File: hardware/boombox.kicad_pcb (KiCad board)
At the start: 4 copper layers, 97.7 x 88.3 mm, 74 parts, among them J1 Micro_SD_Card_Det1, J2 AudioJack4, J3 Battery, J4 USB_C_Receptacle_USB2.0_16P, SW1 SW_SPST, SW2 SW_SPST, SW3 SW_SPST, SW4 SW_SPST, SW5 SW_SPST, U1 Pico, U10 MAX98365A, U2 TMAG5231, U3 TMAG5231, U4 TMAG5231, U5 TMAG5231, U6 TMAG5231, U7 MCP7940MT-I/SN, U8 MAX98365A, U9 MCP73811T-420I-OT, Y1 Crystal

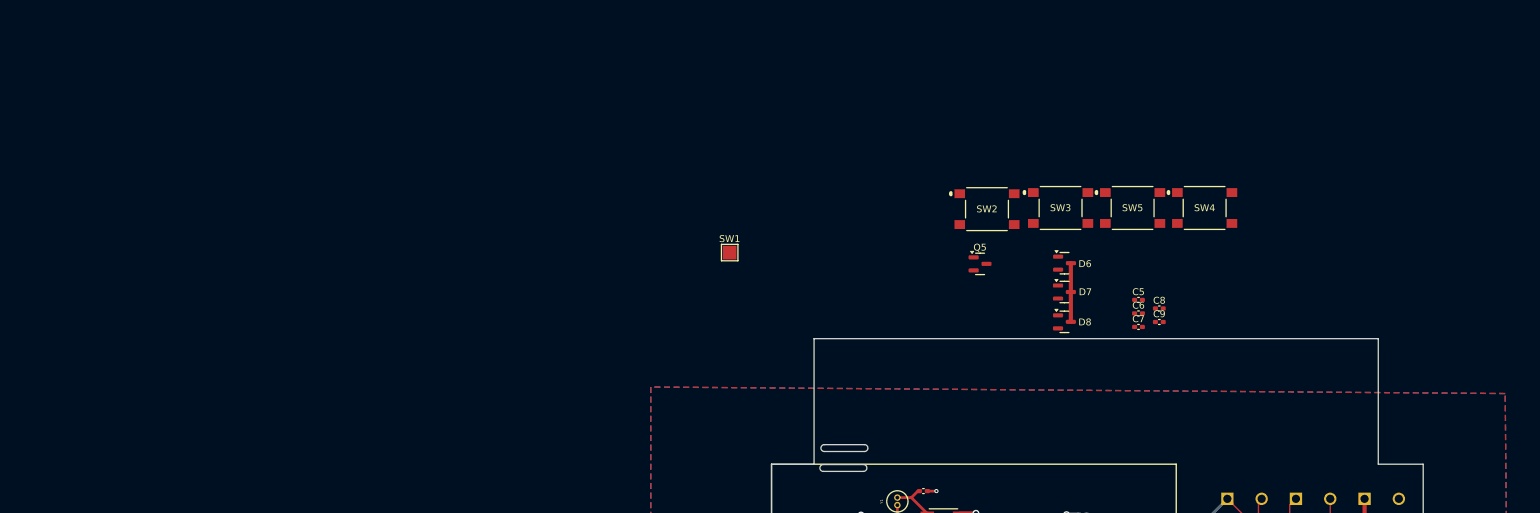
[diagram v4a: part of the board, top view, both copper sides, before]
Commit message: Added button panel
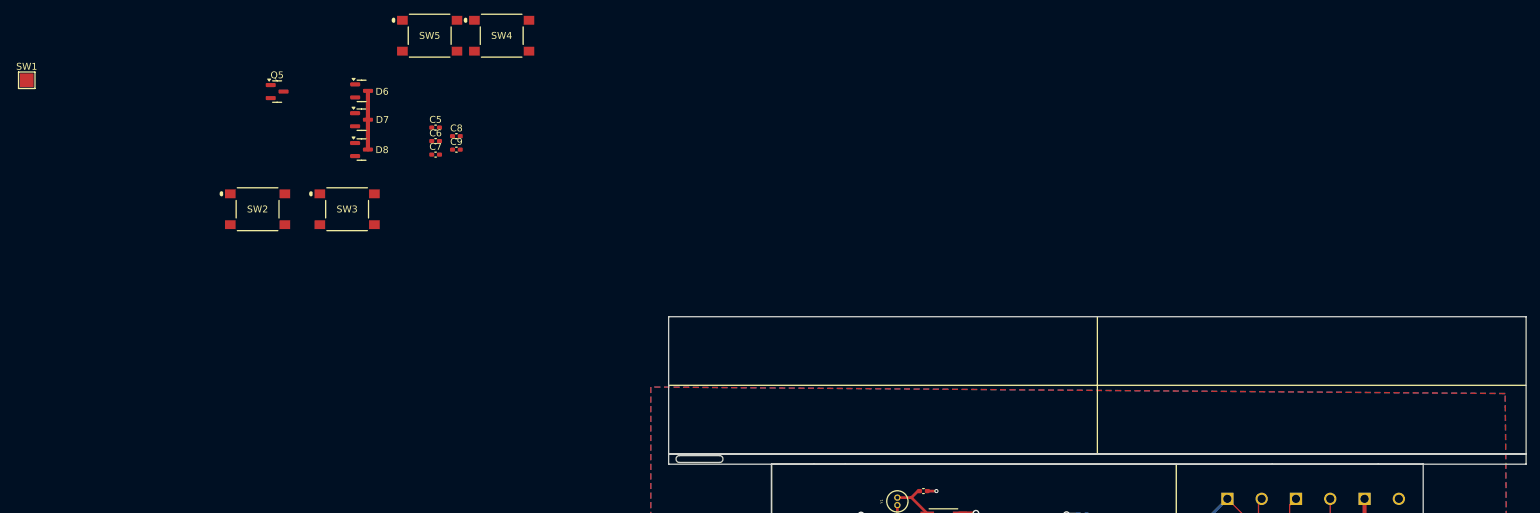
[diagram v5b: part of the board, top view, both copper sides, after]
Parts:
- moved SW2 106.3 mm to (31.5, 30.6)
- moved C5 105.5 mm to (57.4, 18.7)
- moved C6 105.5 mm to (57.4, 20.7)
- moved C7 105.5 mm to (57.4, 22.7)
- moved C8 105.5 mm to (60.5, 20.0)
- moved C9 105.5 mm to (60.5, 22.0)
- moved D6 105.5 mm to (46.6, 13.4)
- moved D7 105.5 mm to (46.6, 17.6)
- moved D8 105.5 mm to (46.6, 21.9)
- moved Q5 105.5 mm to (34.3, 13.5)
- moved SW1 105.5 mm to (-2.17, 11.8)
- moved SW4 105.5 mm to (67.1, 5.33)
- moved SW5 105.5 mm to (56.6, 5.33)
- moved SW3 104.0 mm to (44.5, 30.6)
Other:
- board size 97.7 x 88.3 mm -> 125 x 91.5 mm
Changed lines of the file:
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@@
 	(footprint "Capacitor_SMD:C_0402_1005Metric_Pad0.74x0.62mm_HandSolder"
 		(layer "F.Cu")
-		(at 159.9 45.82)
+		(at 57.428651 20.701301)
 		(descr "Capacitor SMD 0402 (1005 Metric), square (rectangular) end terminal, IPC_7351 nominal with elongated pad for handsoldering. (Body size source: IPC-SM-782 page 76, https://www.pcb-3d.com/wordpress/wp-content/uploads/ipc-sm-782a_amendment_1_and_2.pdf), generated with kicad-footprint-generator")
 		(tags "capacitor handsolder")
@@
 	(footprint "Package_TO_SOT_SMD:SOT-23"
 		(layer "F.Cu")
-		(at 149.1 47.05)
+		(at 46.628651 21.931301)
 		(descr "SOT, 3 Pin (https://www.jedec.org/system/files/docs/to-236h.pdf variant AB), generated with kicad-footprint-generator ipc_gullwing_generator.py")
 		(tags "SOT TO_SOT_SMD")
@@
 	(footprint "boombox:PTS645S_SMTR92_CNK"
 		(layer "F.Cu")
-		(at 148.537498 30.450001)
+		(at 44.528651 30.631301)
 		(tags "PTS645SH50SMTR92LFS ")
 		(property "Reference" "SW3"
@@
 	(footprint "Package_TO_SOT_SMD:SOT-23"
 		(layer "F.Cu")
-		(at 149.1 42.7)
+		(at 46.628651 17.581301)
 		(descr "SOT, 3 Pin (https://www.jedec.org/system/files/docs/to-236h.pdf variant AB), generated with kicad-footprint-generator ipc_gullwing_generator.py")
 		(tags "SOT TO_SOT_SMD")
@@
 	(footprint "boombox:PTS645S_SMTR92_CNK"
 		(layer "F.Cu")
-		(at 159.037498 30.450001)
+		(at 56.566149 5.331302)
 		(tags "PTS645SH50SMTR92LFS ")
 		(property "Reference" "SW5"
@@
 	(footprint "Capacitor_SMD:C_0402_1005Metric_Pad0.74x0.62mm_HandSolder"
 		(layer "F.Cu")
-		(at 162.9325 45.1)
+		(at 60.461151 19.981301)
 		(descr "Capacitor SMD 0402 (1005 Metric), square (rectangular) end terminal, IPC_7351 nominal with elongated pad for handsoldering. (Body size source: IPC-SM-782 page 76, https://www.pcb-3d.com/wordpress/wp-content/uploads/ipc-sm-782a_amendment_1_and_2.pdf), generated with kicad-footprint-generator")
 		(tags "capacitor handsolder")
@@
 	(footprint "Package_TO_SOT_SMD:SOT-23"
 		(layer "F.Cu")
-		(at 136.8 38.6)
+		(at 34.328651 13.481301)
 		(descr "SOT, 3 Pin (https://www.jedec.org/system/files/docs/to-236h.pdf variant AB), generated with kicad-footprint-generator ipc_gullwing_generator.py")
 		(tags "SOT TO_SOT_SMD")
@@
 	(footprint "Capacitor_SMD:C_0402_1005Metric_Pad0.74x0.62mm_HandSolder"
 		(layer "F.Cu")
-		(at 162.9325 47.07)
+		(at 60.461151 21.951301)
 		(descr "Capacitor SMD 0402 (1005 Metric), square (rectangular) end terminal, IPC_7351 nominal with elongated pad for handsoldering. (Body size source: IPC-SM-782 page 76, https://www.pcb-3d.com/wordpress/wp-content/uploads/ipc-sm-782a_amendment_1_and_2.pdf), generated with kicad-footprint-generator")
 		(tags "capacitor handsolder")
@@
 	(footprint "boombox:PTS645S_SMTR92_CNK"
 		(layer "F.Cu")
-		(at 137.808847 30.6187)
+		(at 31.478651 30.631301)
 		(tags "PTS645SH50SMTR92LFS ")
 		(property "Reference" "SW2"
@@
 	(footprint "Capacitor_SMD:C_0402_1005Metric_Pad0.74x0.62mm_HandSolder"
 		(layer "F.Cu")
-		(at 159.9 47.79)
+		(at 57.428651 22.671301)
 		(descr "Capacitor SMD 0402 (1005 Metric), square (rectangular) end terminal, IPC_7351 nominal with elongated pad for handsoldering. (Body size source: IPC-SM-782 page 76, https://www.pcb-3d.com/wordpress/wp-content/uploads/ipc-sm-782a_amendment_1_and_2.pdf), generated with kicad-footprint-generator")
 		(tags "capacitor handsolder")
@@
 	(footprint "Capacitor_SMD:C_0402_1005Metric_Pad0.74x0.62mm_HandSolder"
 		(layer "F.Cu")
-		(at 159.9 43.85)
+		(at 57.428651 18.731301)
 		(descr "Capacitor SMD 0402 (1005 Metric), square (rectangular) end terminal, IPC_7351 nominal with elongated pad for handsoldering. (Body size source: IPC-SM-782 page 76, https://www.pcb-3d.com/wordpress/wp-content/uploads/ipc-sm-782a_amendment_1_and_2.pdf), generated with kicad-footprint-generator")
 		(tags "capacitor handsolder")
@@
 	(footprint "Package_TO_SOT_SMD:SOT-23"
 		(layer "F.Cu")
-		(at 149.1125 38.5)
+		(at 46.641151 13.381301)
 		(descr "SOT, 3 Pin (https://www.jedec.org/system/files/docs/to-236h.pdf variant AB), generated with kicad-footprint-generator ipc_gullwing_generator.py")
 		(tags "SOT TO_SOT_SMD")
@@
 	(footprint "boombox:PTS645S_SMTR92_CNK"
 		(layer "F.Cu")
-		(at 169.537498 30.450001)
+		(at 67.066149 5.331302)
 		(tags "PTS645SH50SMTR92LFS ")
 		(property "Reference" "SW4"
@@
 	(footprint "TestPoint:TestPoint_Pad_2.0x2.0mm"
 		(layer "F.Cu")
-		(at 100.3 36.95)
+		(at -2.171349 11.831301)
 		(descr "SMD rectangular pad as test Point, square 2.0mm side length")
 		(tags "test point SMD pad rectangle square")
@@
 		(layer "F.SilkS")
 	)
-	(gr_arc
-		(start 119.95 64.95)
-		(mid 120.45 65.45)
-		(end 119.95 65.95)
+	(gr_line
+		(start 153.9 46.3)
+		(end 153.9 66.3)
 		(stroke
 			(width 0.05)
 			(type default)
 		)
-		(layer "Edge.Cuts")
+		(layer "F.SilkS")
 	)
-	(gr_arc
-		(start 114.1 65.95)
-		(mid 113.6 65.45)
-		(end 114.1 64.95)
+	(gr_line
+		(start 91.4 56.3)
+		(end 216.4 56.3)
 		(stroke
 			(width 0.05)
 			(type default)
 		)
-		(layer "Edge.Cuts")
+		(layer "F.SilkS")
 	)
-	(gr_line
-		(start 113.95 68.85)
-		(end 119.8 68.85)
+	(gr_arc
+		(start 98.825 66.55)
+		(mid 99.325 67.05)
+		(end 98.825 67.55)
 		(stroke
 			(width 0.05)
@@
 		(layer "Edge.Cuts")
 	)
-	(gr_line
-		(start 114.1 64.95)
-		(end 119.95 64.95)
+	(gr_rect
+		(start 91.4 46.3)
+		(end 216.4 66.3)
 		(stroke
 			(width 0.05)
 			(type default)
 		)
+		(fill none)
 		(layer "Edge.Cuts")
 	)
-	(gr_line
-		(start 114.1 65.95)
-		(end 119.95 65.95)
+	(gr_arc
+		(start 92.975 67.55)
+		(mid 92.475 67.05)
+		(end 92.975 66.55)
 		(stroke
 			(width 0.05)
@@
 		(layer "Edge.Cuts")
 	)
-	(gr_arc
-		(start 113.95 68.85)
-		(mid 113.45 68.35)
-		(end 113.95 67.85)
+	(gr_line
+		(start 92.975 66.55)
+		(end 98.825 66.55)
 		(stroke
 			(width 0.05)
@@
 		(layer "Edge.Cuts")
 	)
-	(gr_poly
-		(pts
-			(xy 201.4 120.95) (xy 204.125 120.95) (xy 204.125 132.05) (xy 201.4 132.05) (xy 201.4 137.8) (xy 106.4 137.8)
-			(xy 106.4 67.8) (xy 112.6 67.8) (xy 112.6 49.5) (xy 194.85 49.5) (xy 194.85 67.8) (xy 201.4 67.8)
-		)
+	(gr_line
+		(start 92.975 67.55)
+		(end 98.825 67.55)
 		(stroke
 			(width 0.05)
 			(type default)
 		)
-		(fill none)
 		(layer "Edge.Cuts")
 	)
-	(gr_line
-		(start 113.95 67.85)
-		(end 119.8 67.85)
+	(gr_rect
+		(start 91.4 66.3)
+		(end 216.4 67.8)
 		(stroke
 			(width 0.05)
 			(type default)
 		)
+		(fill none)
 		(layer "Edge.Cuts")
 	)
-	(gr_arc
-		(start 119.8 67.85)
-		(mid 120.3 68.35)
-		(end 119.8 68.85)
+	(gr_poly
+		(pts
+			(xy 201.4 120.95) (xy 204.125 120.95) (xy 204.125 132.05) (xy 201.4 132.05) (xy 201.4 137.8) (xy 106.4 137.8)
+			(xy 106.4 67.8) (xy 112.6 67.8) (xy 117.15 67.8) (xy 179.4 67.8) (xy 194.85 67.8) (xy 201.4 67.8)
+		)
 		(stroke
 			(width 0.05)
 			(type default)
 		)
+		(fill none)
 		(layer "Edge.Cuts")
 	)
@@
 	)
 	(segment
-		(start 150.0375 47.05)
-		(end 150.0375 42.7)
+		(start 47.566151 21.931301)
+		(end 47.566151 17.581301)
 		(width 0.6)
 		(layer "F.Cu")
@@
 	)
 	(segment
-		(start 150.0375 42.7)
-		(end 150.0375 38.5125)
+		(start 47.566151 17.581301)
+		(end 47.566151 13.393801)
 		(width 0.6)
 		(layer "F.Cu")
@@
 	)
 	(segment
-		(start 150.0375 38.5125)
-		(end 150.05 38.5)
+		(start 47.566151 13.393801)
+		(end 47.578651 13.381301)
 		(width 0.6)
 		(layer "F.Cu")

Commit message: Switches
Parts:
- removed R15: 0, Resistor_SMD:R_0402_1005Metric_Pad0.72x0.64mm_HandSolder
- added R12: 0, Resistor_SMD:R_0402_1005Metric_Pad0.72x0.64mm_HandSolder, B.Cu at (163.3, 105.3)
- added R5: 1M, Resistor_SMD:R_0402_1005Metric_Pad0.72x0.64mm_HandSolder, F.Cu at (116.2, 75.2)
- added TP1: ~, boombox:TestPoint_Pad_2.0x2.0mm, F.Cu at (139.8, 62.5)
- added TP10: ~, boombox:TestPoint_Pad_2.0x2.0mm, F.Cu at (90.9, 91.2)
- added TP11: TestPoint_Small, boombox:TestPoint_Pad_2.0x2.0mm, F.Cu at (85.1, 68.7)
- added TP12: TestPoint_Small, boombox:TestPoint_Pad_2.0x2.0mm, F.Cu at (85.1, 64.6)
- added TP2: ~, boombox:TestPoint_Pad_2.0x2.0mm, F.Cu at (86.8, 79.1)
- added TP3: ~, boombox:TestPoint_Pad_2.0x2.0mm, F.Cu at (143.4, 62.5)
- added TP4: ~, boombox:TestPoint_Pad_2.0x2.0mm, F.Cu at (86.8, 87.2)
- added TP5: ~, boombox:TestPoint_Pad_2.0x2.0mm, B.Cu at (149.8, 62.8)
- added TP6: ~, boombox:TestPoint_Pad_2.0x2.0mm, F.Cu at (68.5, 14.6)
- added TP7: ~, boombox:TestPoint_Pad_2.0x2.0mm, F.Cu at (157.5, 63.7)
- added TP8: ~, boombox:TestPoint_Pad_2.0x2.0mm, F.Cu at (90.9, 83.2)
- added TP9: ~, boombox:TestPoint_Pad_2.0x2.0mm, F.Cu at (161.0, 63.8)
- C10: moved to B.Cu
- SW1: footprint TestPoint:TestPoint_Pad_2.0x2.0mm -> boombox:PTS645S_SMTR92_CNK
- moved SW5 150.2 mm to (197.9, 56.3)
- moved SW1 120.6 mm to (109.9, 56.3)
- moved SW4 120.2 mm to (175.9, 56.3)
- moved SW3 112.3 mm to (153.9, 56.3)
- moved SW2 103.7 mm to (131.9, 56.3)
- moved C7 102.8 mm to (148.9, 69.7)
- moved C10 65.1 mm to (148.7, 105.9), turned to 180 degrees
- moved C17 40.7 mm to (126.0, 122.5)
- moved C11 40.6 mm to (126.0, 125.0)
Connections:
- C5 pad 1: /Power/BUTTONS0 -> Net-(SW1-A)
- C6 pad 1: /Power/BUTTONS1 -> Net-(SW2-A)
- C7 pad 1: /Power/BUTTONS2 -> Net-(SW3-A)
- C8 pad 1: /Power/BUTTONS3 -> Net-(SW4-A)
- C9 pad 1: /Power/BUTTONS4 -> Net-(SW5-A)
- SW1 pad 1: /Power/BUTTONS0 -> Net-(SW1-A)
- SW2 pad 1: /Power/BUTTONS1 -> Net-(SW2-A)
- SW2 pad 2: SLP_PWR -> BTN_PWR
- SW3 pad 1: /Power/BUTTONS2 -> Net-(SW3-A)
- SW3 pad 2: SLP_PWR -> BTN_PWR
- SW4 pad 1: /Power/BUTTONS3 -> Net-(SW4-A)
- SW4 pad 2: SLP_PWR -> BTN_PWR
- SW5 pad 1: /Power/BUTTONS4 -> Net-(SW5-A)
- SW5 pad 2: SLP_PWR -> BTN_PWR
- U1 pad 15: /Power/BUTTONS0 -> Net-(SW1-A)
- U1 pad 16: /Power/BUTTONS1 -> Net-(SW2-A)
- U1 pad 17: /Power/BUTTONS2 -> Net-(SW3-A)
- U1 pad 19: /Power/BUTTONS3 -> Net-(SW4-A)
- U1 pad 20: /Power/BUTTONS4 -> Net-(SW5-A)
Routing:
- net Net-(D1A-K): track 73.1 -> 81.6 mm
- net GND: track 62.0 -> 70.1 mm, vias 31 -> 33
- net SLP_PWR: track 239.5 -> 244.3 mm
- net Net-(J1-VDD): track 60.9 -> 65.1 mm, vias 1 -> 2
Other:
- outline, holes or cut-outs redrawn
